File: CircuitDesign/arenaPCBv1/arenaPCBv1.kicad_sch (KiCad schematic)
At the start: 25 parts, among them Q1 IRLB3034

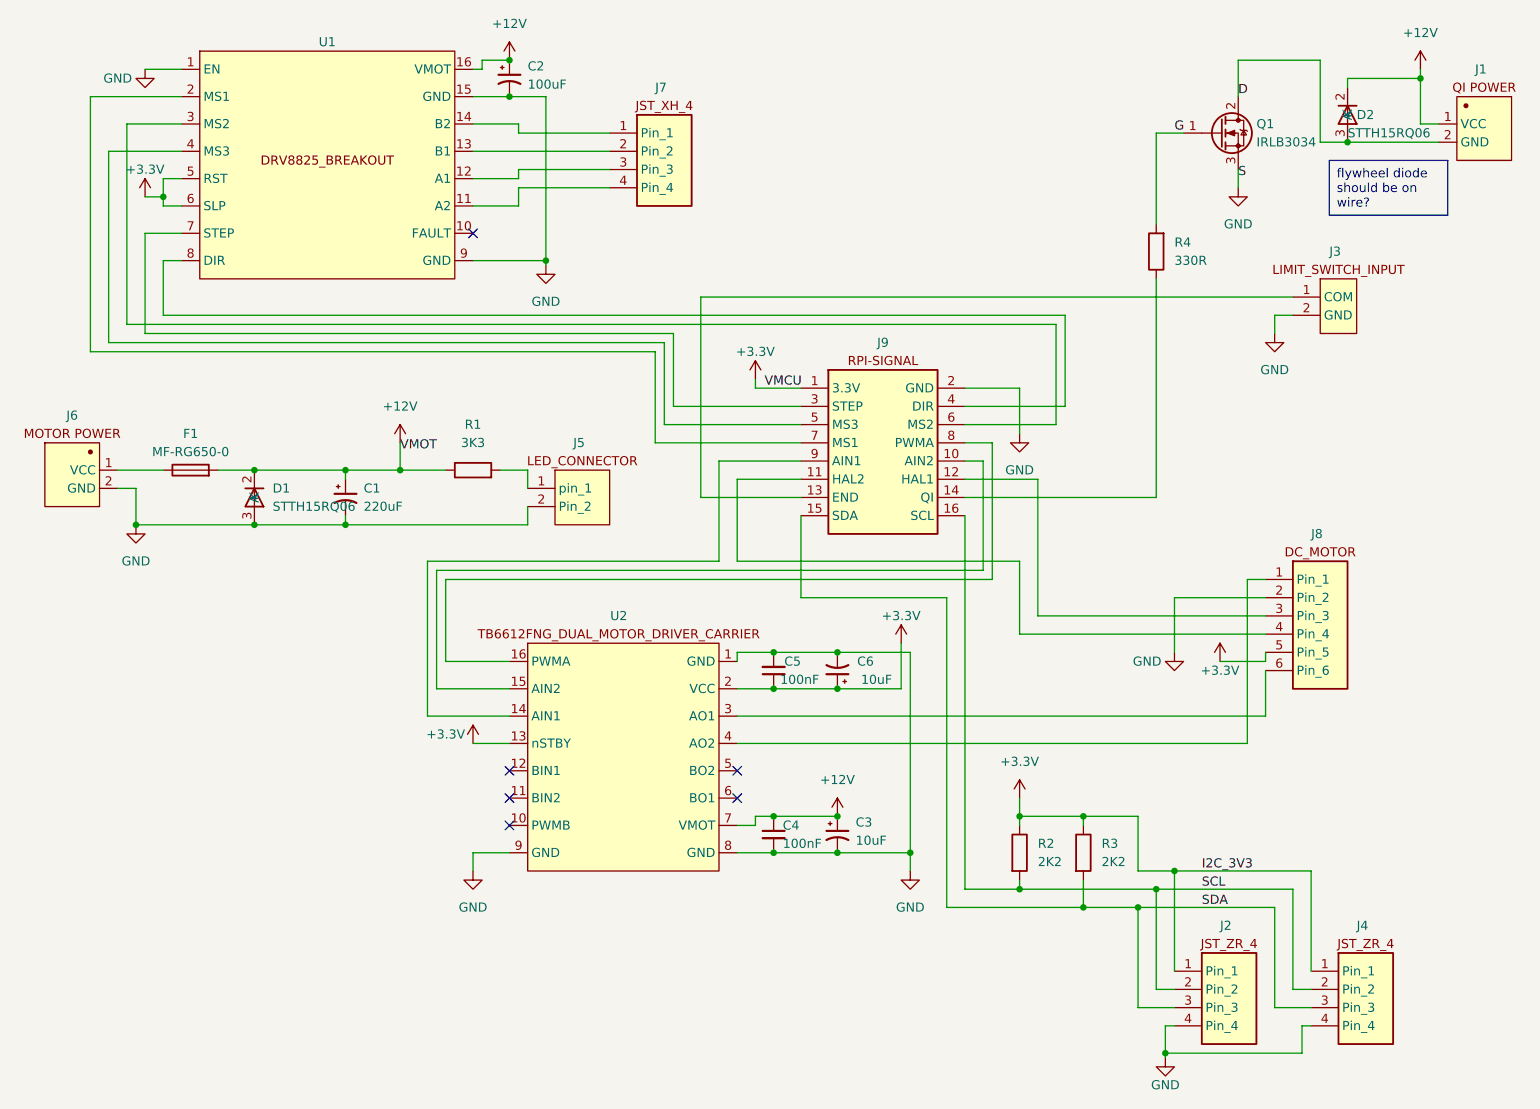
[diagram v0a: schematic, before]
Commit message: pcb done before changing diodes and C1
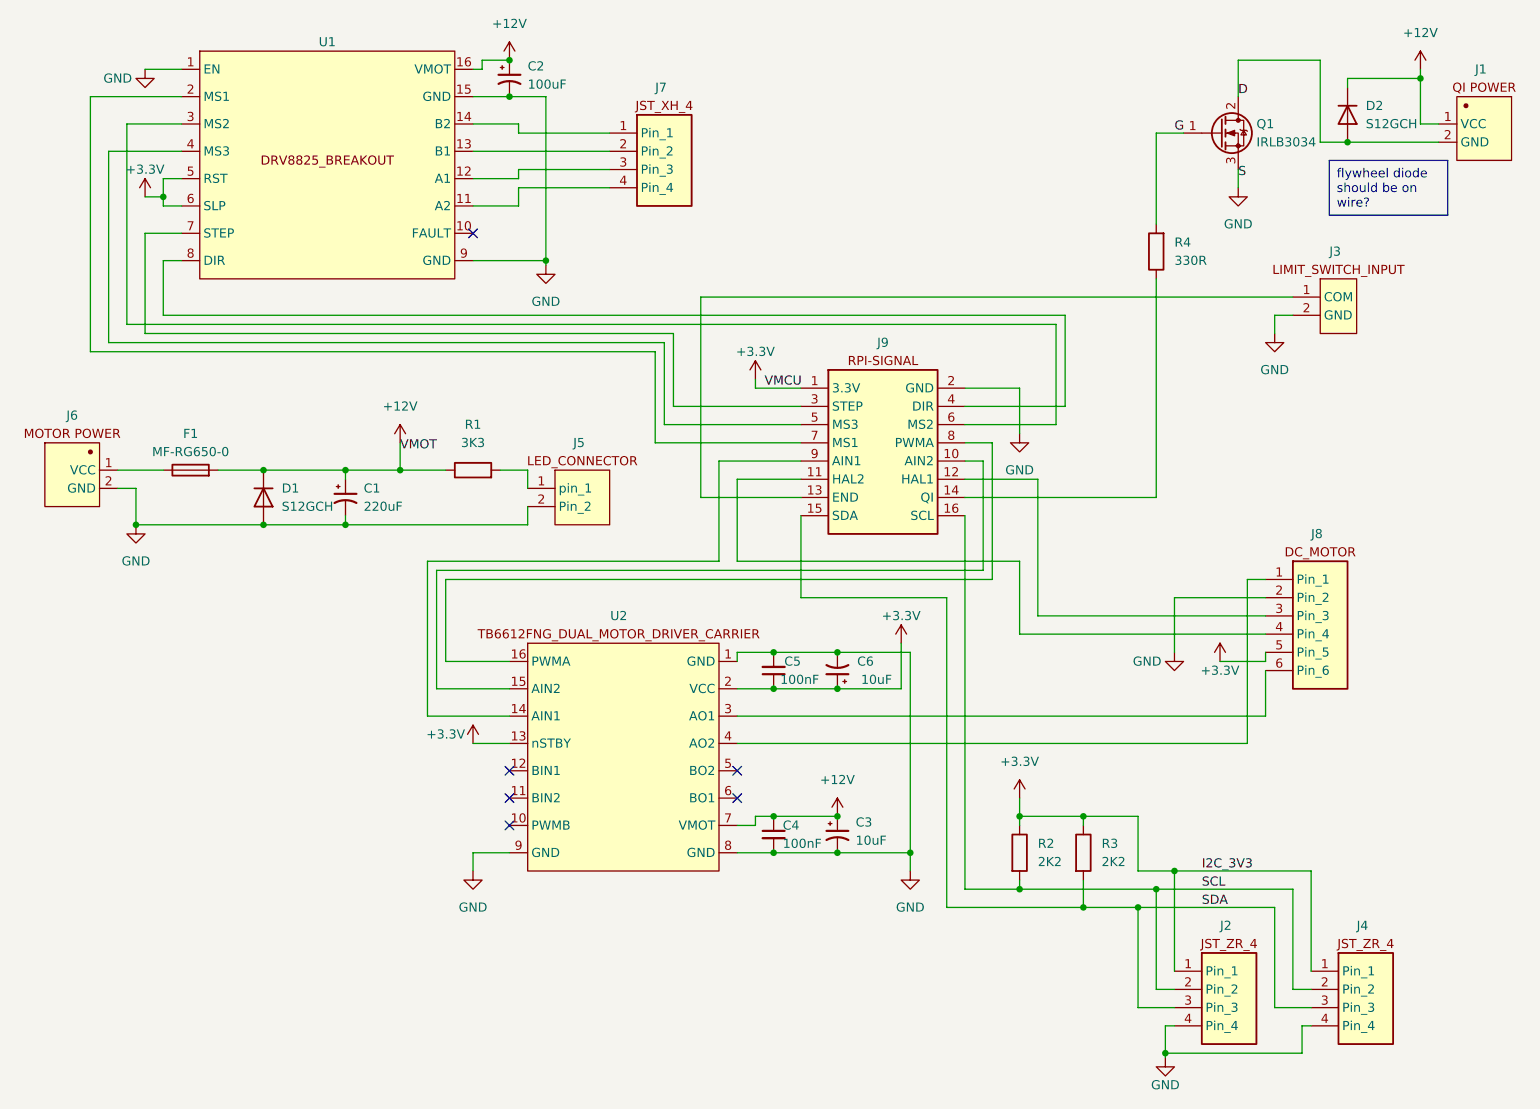
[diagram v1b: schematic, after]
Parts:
- removed D1, D2: STTH15RQ06, Package_TO_SOT_SMD:TO-263-2, symbol 1_Bachelors_Symbols:Diode_D2PAK
- added D1, D2: S12GCH, 2_Bachelors_footprints:S12GCH, symbol Device:D
- C1: footprint Capacitor_THT:CP_Radial_D10.0mm_P5.00mm -> Capacitor_SMD:CP_Elec_10x10.5
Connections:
- net +12V: now also D1.1 (K), D2.1 (K)
- net D: now also D2.2 (A)
- net GND: now also D1.2 (A)
